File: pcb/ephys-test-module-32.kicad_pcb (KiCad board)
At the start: 2 copper layers, 100 x 60 mm, 11 parts, among them J2 BSE-040-01-F-D-A-TR, J3 BSE-040-01-F-D-A-TR, J4 2x2 header, J5 A79026-001, U1 AT24C64D-SSHM-T

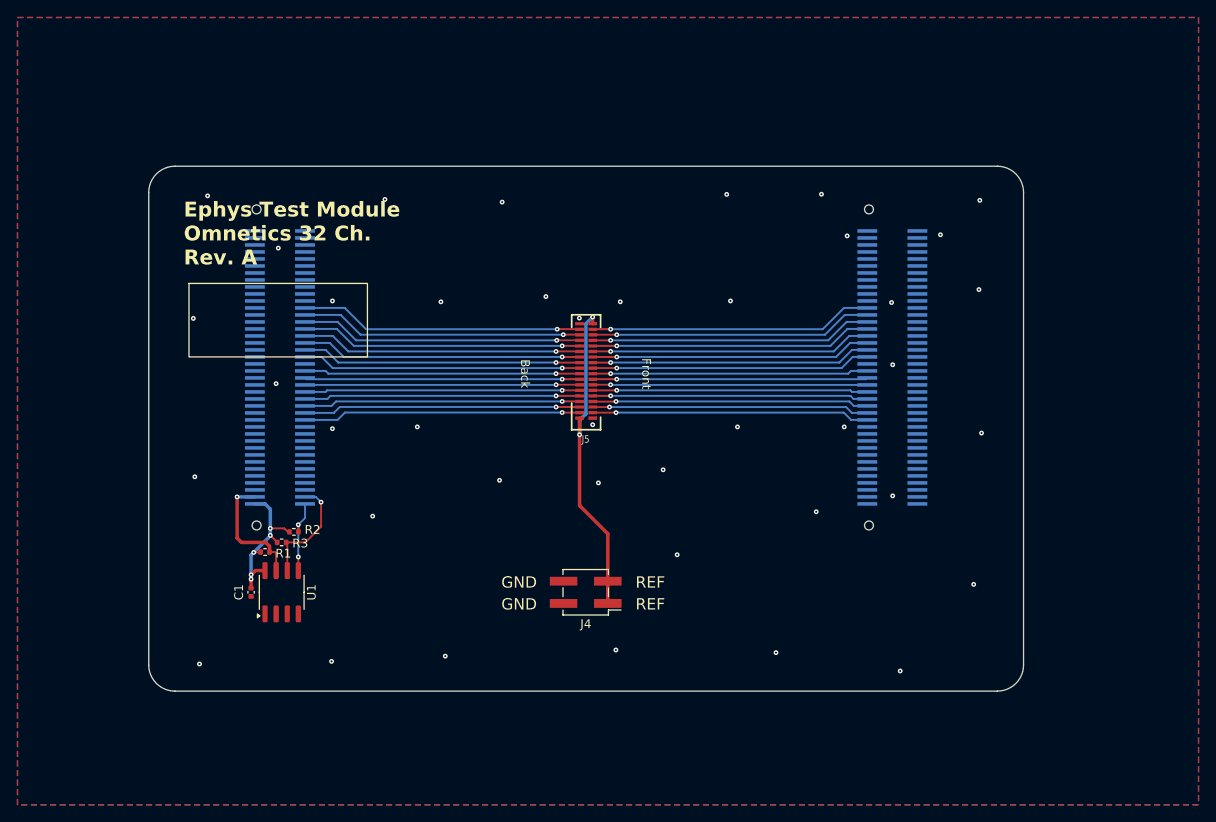
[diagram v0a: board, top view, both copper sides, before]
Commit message: updates
10R line resistors on IOs
Logo & name position
barcode position
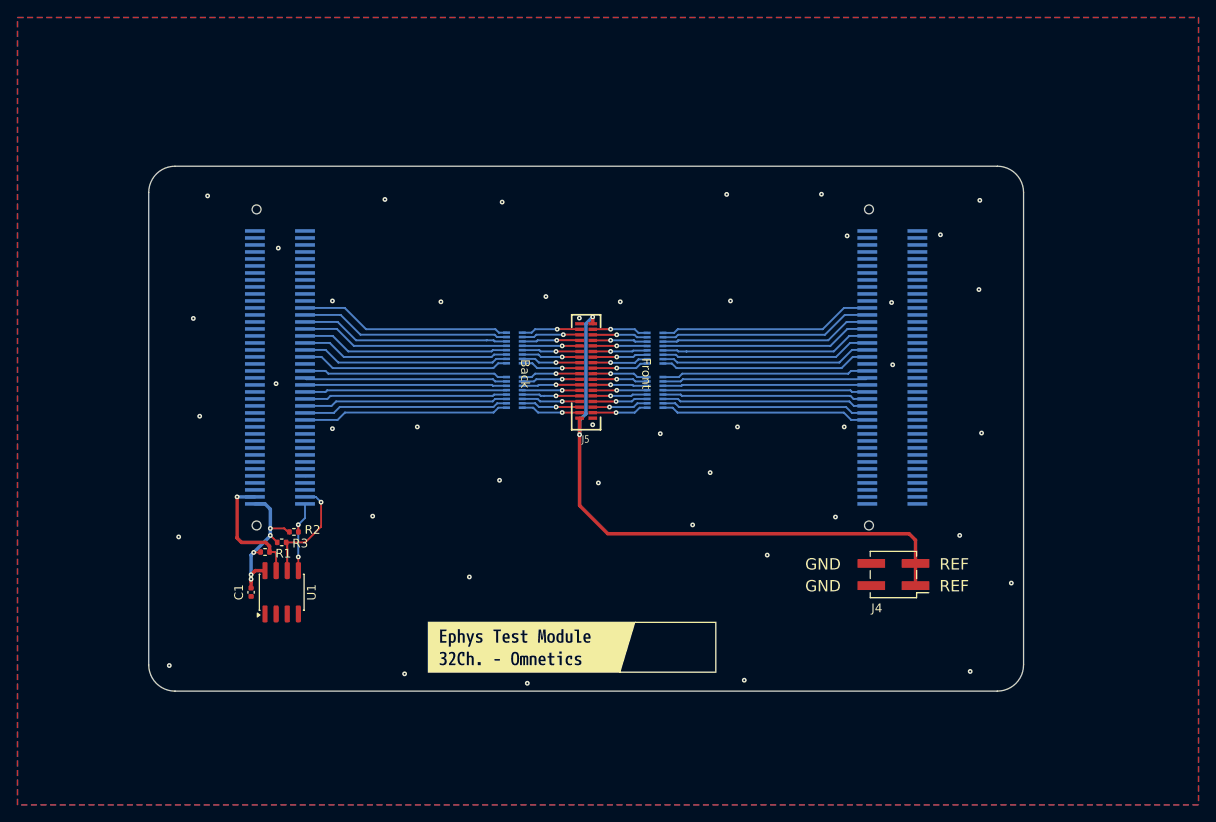
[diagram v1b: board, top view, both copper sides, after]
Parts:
- added G***: LOGO, LOGO, F.Cu at (167.9, 132.0)
- added RN1: 100k, Resistor_SMD:R_Array_Convex_8x0602, B.Cu at (149.8, 102.8)
- added RN2: 100k, Resistor_SMD:R_Array_Convex_8x0602, B.Cu at (165.9, 102.8)
- added RN3: 100k, Resistor_SMD:R_Array_Convex_8x0602, B.Cu at (149.8, 97.8)
- added RN4: 100k, Resistor_SMD:R_Array_Convex_8x0602, B.Cu at (165.9, 97.8)
- added kibuzzard-69C29391: G***, kibuzzard-69C29391, F.Cu at (151.8, 132.0)
- H1: moved to B.Cu
- moved H1 36.7 mm to (123.7, 131.3), turned to 180 degrees
- moved J4 35.2 mm to (193.1, 123.7)
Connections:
- J5 pad 10: /Headstage Interface/B10.E_{4} -> /Headstage Interface/E23
- J5 pad 11: /Headstage Interface/B6.E_{3} -> /Headstage Interface/E24
- J5 pad 12: /Headstage Interface/B10.E_{3} -> /Headstage Interface/E25
- J5 pad 13: /Headstage Interface/B6.E_{2} -> /Headstage Interface/E26
- J5 pad 14: /Headstage Interface/B10.E_{2} -> /Headstage Interface/E27
- J5 pad 15: /Headstage Interface/B6.E_{1} -> /Headstage Interface/E28
- J5 pad 16: /Headstage Interface/B10.E_{1} -> /Headstage Interface/E29
- J5 pad 17: /Headstage Interface/B6.E_{0} -> /Headstage Interface/E30
- J5 pad 18: /Headstage Interface/B10.E_{0} -> /Headstage Interface/E31
- J5 pad 19: /Headstage Interface/B5.E_{7} -> /Headstage Interface/E32
- J5 pad 20: /Headstage Interface/B9.E_{7} -> /Headstage Interface/E33
- J5 pad 21: /Headstage Interface/B5.E_{6} -> /Headstage Interface/E34
- J5 pad 22: /Headstage Interface/B9.E_{6} -> /Headstage Interface/E35
- J5 pad 23: /Headstage Interface/B5.E_{5} -> /Headstage Interface/E36
- J5 pad 24: /Headstage Interface/B9.E_{5} -> /Headstage Interface/E37
- J5 pad 25: /Headstage Interface/B5.E_{4} -> /Headstage Interface/E38
- J5 pad 26: /Headstage Interface/B9.E_{4} -> /Headstage Interface/E39
- J5 pad 27: /Headstage Interface/B5.E_{3} -> /Headstage Interface/E40
- J5 pad 28: /Headstage Interface/B9.E_{3} -> /Headstage Interface/E41
- J5 pad 29: /Headstage Interface/B5.E_{2} -> /Headstage Interface/E42
- J5 pad 3: /Headstage Interface/B6.E_{7} -> /Headstage Interface/E16
- J5 pad 30: /Headstage Interface/B9.E_{2} -> /Headstage Interface/E43
- J5 pad 31: /Headstage Interface/B5.E_{1} -> /Headstage Interface/E44
- J5 pad 32: /Headstage Interface/B9.E_{1} -> /Headstage Interface/E45
- J5 pad 33: /Headstage Interface/B5.E_{0} -> /Headstage Interface/E46
- J5 pad 34: /Headstage Interface/B9.E_{0} -> /Headstage Interface/E47
- J5 pad 4: /Headstage Interface/B10.E_{7} -> /Headstage Interface/E17
- J5 pad 5: /Headstage Interface/B6.E_{6} -> /Headstage Interface/E18
- J5 pad 6: /Headstage Interface/B10.E_{6} -> /Headstage Interface/E19
- J5 pad 7: /Headstage Interface/B6.E_{5} -> /Headstage Interface/E20
- J5 pad 8: /Headstage Interface/B10.E_{5} -> /Headstage Interface/E21
- J5 pad 9: /Headstage Interface/B6.E_{4} -> /Headstage Interface/E22
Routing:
- net /Headstage Interface/REF: track 37.4 -> 70.1 mm
- net /Headstage Interface/B5.E_{3}: track 32.3 -> 23.8 mm, vias 1 -> 0
- net /Headstage Interface/B6.E_{3}: track 31.5 -> 23.1 mm, vias 1 -> 0
- net /Headstage Interface/B6.E_{2}: track 31.5 -> 23.1 mm, vias 1 -> 0
- net /Headstage Interface/B5.E_{2}: track 32.3 -> 24.0 mm, vias 1 -> 0
- net /Headstage Interface/B5.E_{4}: track 32.2 -> 23.8 mm, vias 1 -> 0
- net /Headstage Interface/B6.E_{4}: track 31.6 -> 23.2 mm, vias 1 -> 0
- net /Headstage Interface/B6.E_{1}: track 31.5 -> 23.2 mm, vias 1 -> 0
- net /Headstage Interface/B5.E_{1}: track 32.4 -> 24.1 mm, vias 1 -> 0
- net /Headstage Interface/B5.E_{5}: track 32.1 -> 23.8 mm, vias 1 -> 0
- net /Headstage Interface/B6.E_{5}: track 31.7 -> 23.4 mm, vias 1 -> 0
- net /Headstage Interface/B5.E_{0}: track 32.5 -> 24.2 mm, vias 1 -> 0
- net /Headstage Interface/B6.E_{0}: track 31.6 -> 23.3 mm, vias 1 -> 0
- net /Headstage Interface/B5.E_{6}: track 32.0 -> 23.8 mm, vias 1 -> 0
- net /Headstage Interface/B6.E_{6}: track 31.7 -> 23.5 mm, vias 1 -> 0
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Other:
- board text removed: "Ephys Test Module Omnetics 32 Ch. Rev. A"

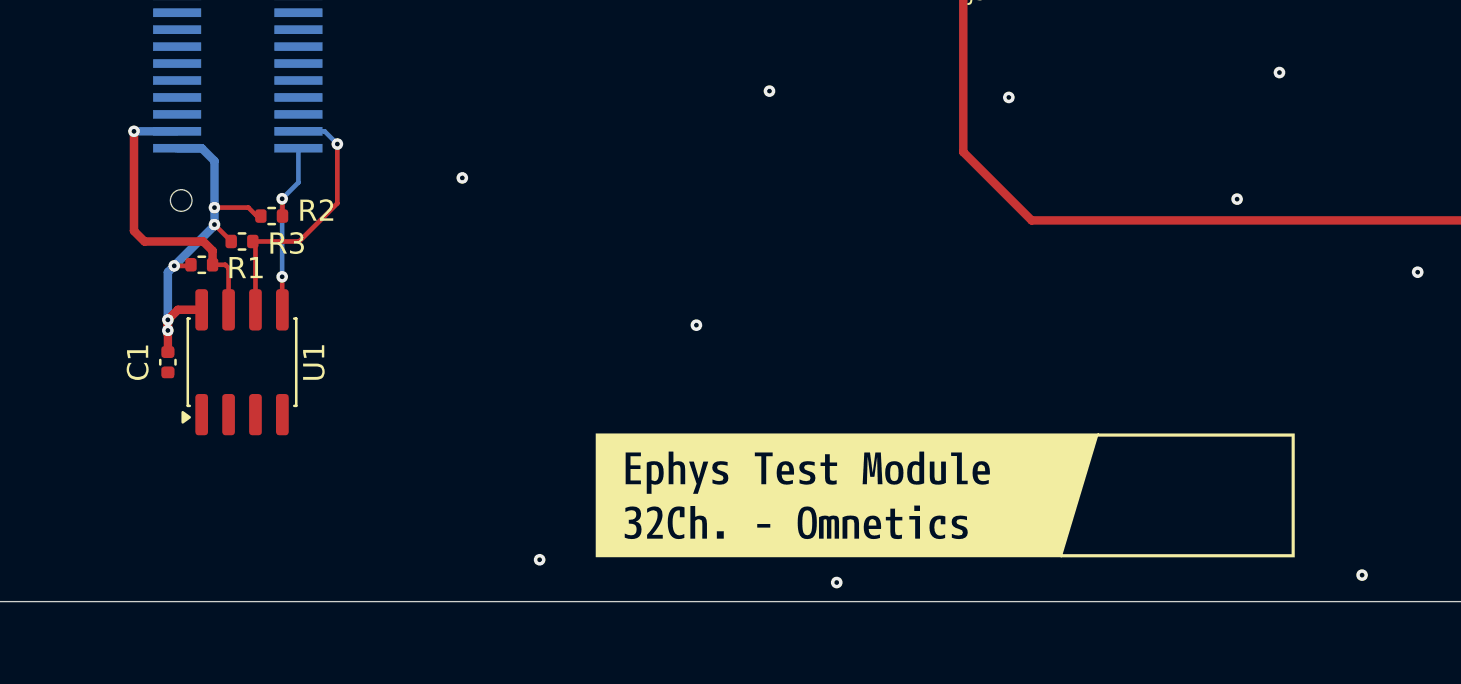
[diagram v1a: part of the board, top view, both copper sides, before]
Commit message: tunning em designators
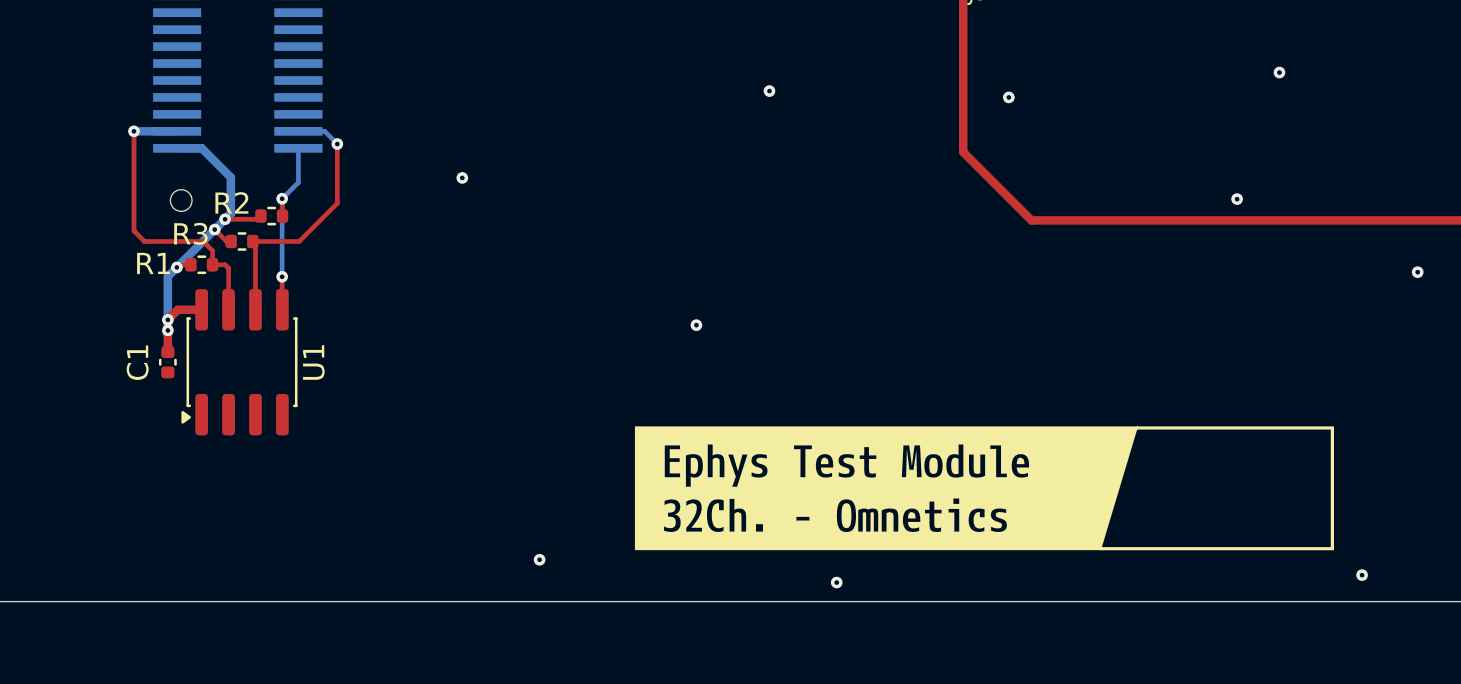
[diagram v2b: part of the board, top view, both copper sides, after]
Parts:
- removed the G*** at (194.0, 87.0)
- moved H1 3.16 mm to (123.2, 128.2)
- moved G*** 1.88 mm to (169.8, 131.6)
- moved kibuzzard-69C29391 1.88 mm to (153.6, 131.7)
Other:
- board text added: "Rev. B"

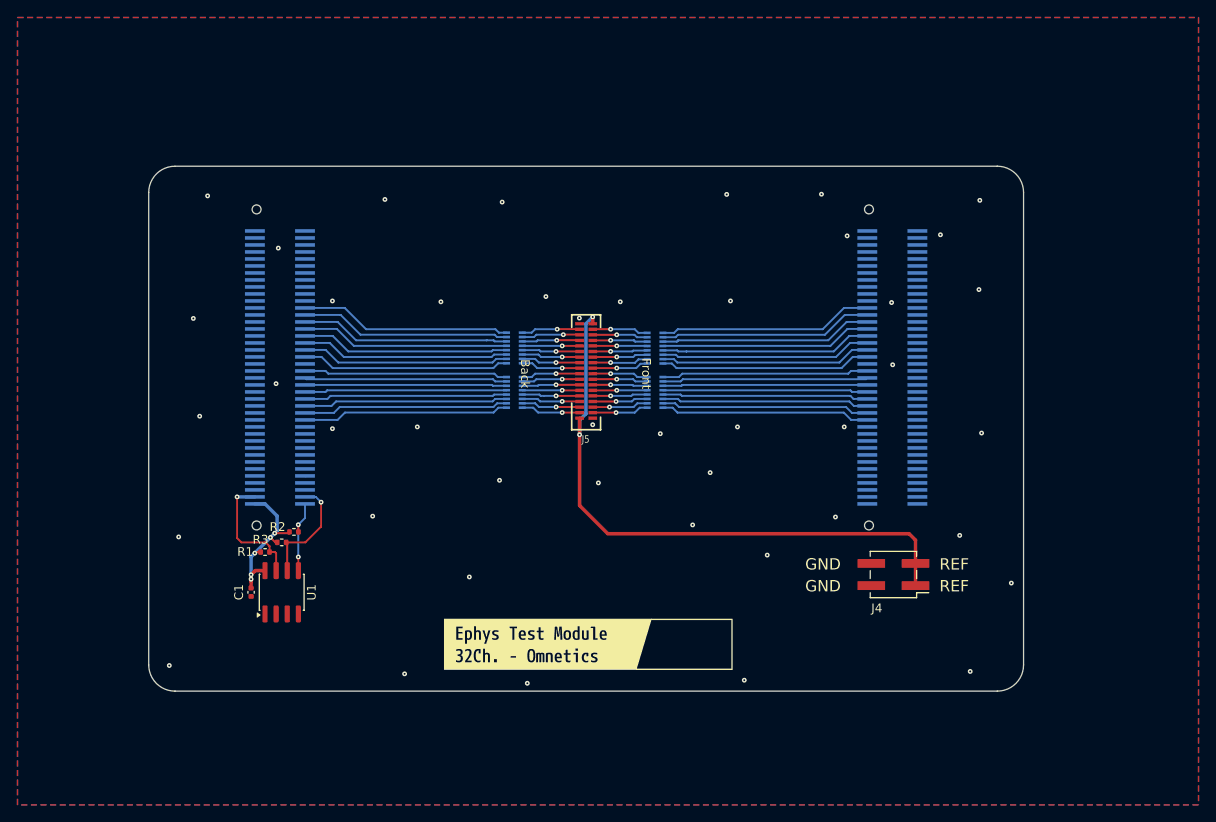
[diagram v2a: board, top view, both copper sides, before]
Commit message: details & manufacturing files
- chaged via size D=0.5mm & H=0.2mm
- generated production files
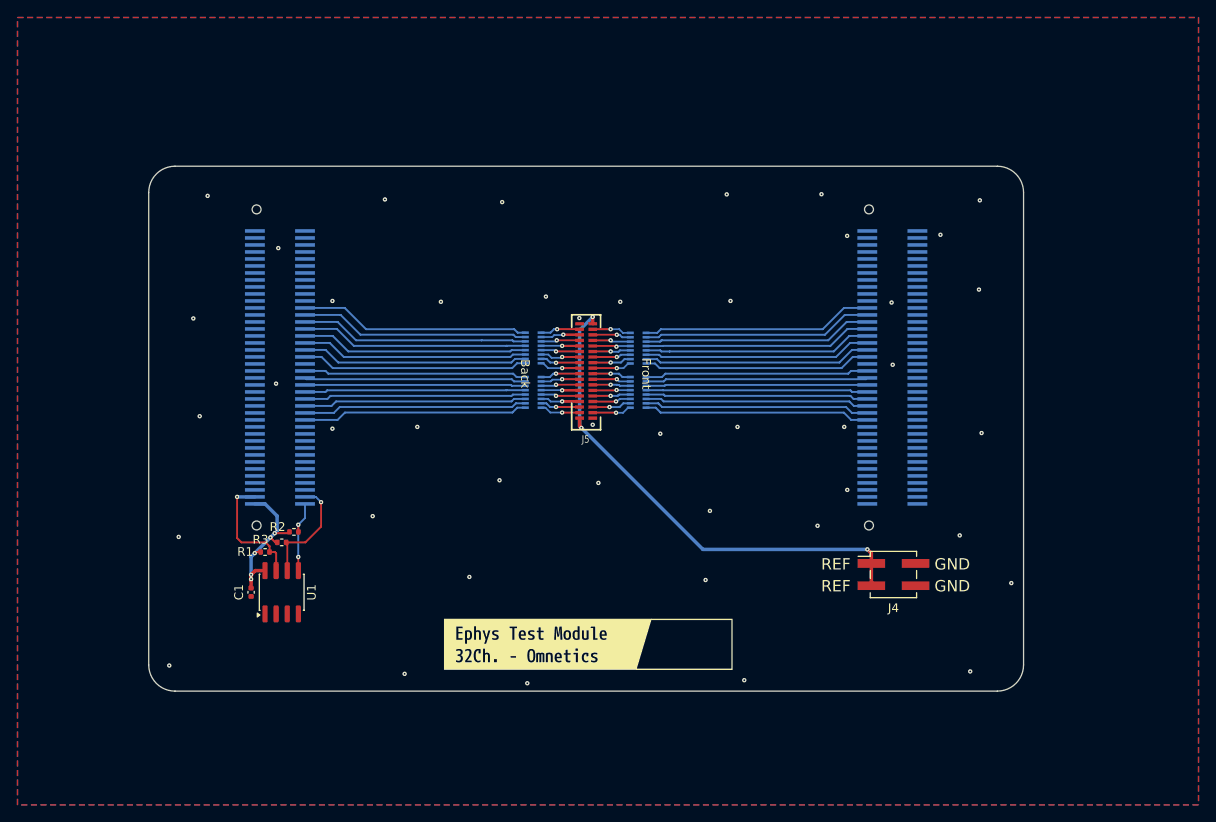
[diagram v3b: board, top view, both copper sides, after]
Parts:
- J4: value 2x2 header -> M20-8760242
- moved RN1 2.15 mm to (151.9, 102.8)
- moved RN3 2.15 mm to (151.9, 97.8)
- moved RN2 1.93 mm to (163.9, 102.8)
- moved RN4 1.93 mm to (163.9, 97.8)
- turned J4 to 0 degrees
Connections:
- J3 pad 77: GND -> unconnected-(J3-Pin_77-Pad77)
- J3 pad 78: GND -> unconnected-(J3-Pin_78-Pad78)
- J3 pad 79: GND -> unconnected-(J3-Pin_79-Pad79)
- J3 pad 80: GND -> unconnected-(J3-Pin_80-Pad80)
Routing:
- net /Headstage Interface/REF: track 70.1 -> 58.1 mm, vias 2 -> 3
- net /Headstage Interface/E46: track 6.82 -> 4.64 mm
- net /Headstage Interface/E30: track 6.77 -> 4.61 mm
- net /Headstage Interface/E18: track 6.79 -> 4.62 mm
- net /Headstage Interface/E38: track 6.67 -> 4.51 mm
- net /Headstage Interface/E28: track 6.72 -> 4.56 mm
- net /Headstage Interface/E26: track 6.66 -> 4.50 mm
- net /Headstage Interface/E22: track 6.68 -> 4.51 mm
- net /Headstage Interface/E16: track 6.84 -> 4.68 mm
- net /Headstage Interface/B5.E_{2}: track 24.0 -> 26.1 mm
- net /Headstage Interface/B6.E_{6}: track 23.5 -> 25.6 mm
- net /Headstage Interface/B6.E_{5}: track 23.4 -> 25.5 mm
- net /Headstage Interface/B6.E_{3}: track 23.1 -> 25.3 mm
- net /Headstage Interface/B6.E_{2}: track 23.1 -> 25.2 mm
- net /Headstage Interface/B6.E_{1}: track 23.2 -> 25.4 mm
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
